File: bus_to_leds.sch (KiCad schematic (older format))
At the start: 32 parts

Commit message: ram pcb
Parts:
- R0: renamed from R1; value 220 -> 5k
- R1: renamed from R2; value 220 -> 5k
- R10: renamed from R11; value 220 -> 5k
- R11: renamed from R12; value 220 -> 5k
- R12: renamed from R13; value 220 -> 5k
- R13: renamed from R14; value 220 -> 5k
- R14: renamed from R15; value 220 -> 5k
- R15: renamed from R16; value 220 -> 5k
- R2: renamed from R3; value 220 -> 5k
- R3: renamed from R4; value 220 -> 5k
- R4: renamed from R5; value 220 -> 5k
- R5: renamed from R6; value 220 -> 5k
- R6: renamed from R7; value 220 -> 5k
- R7: renamed from R8; value 220 -> 5k
- R8: renamed from R9; value 220 -> 5k
- R9: renamed from R10; value 220 -> 5k
- renumbered D1 to D0, D2 to D1, D11 to D10, D12 to D11, D13 to D12, D14 to D13, D15 to D14, D16 to D15, D3 to D2, D4 to D3, D5 to D4, D6 to D5, D7 to D6, D8 to D7, D9 to D8, D10 to D9

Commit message: way to long since last commit
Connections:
- net D0: now also D15.2 (A); no longer D0.2 (A)
- net D1: now also D14.2 (A); no longer D1.2 (A)
- net D10: now also D5.2 (A); no longer D10.2 (A)
- net D11: now also D4.2 (A); no longer D11.2 (A)
- net D12: now also D3.2 (A); no longer D12.2 (A)
- net D13: now also D2.2 (A); no longer D13.2 (A)
- net D14: now also D1.2 (A); no longer D14.2 (A)
- net D15: now also D0.2 (A); no longer D15.2 (A)
- net D2: now also D13.2 (A); no longer D2.2 (A)
- net D3: now also D12.2 (A); no longer D3.2 (A)
- net D4: now also D11.2 (A); no longer D4.2 (A)
- net D5: now also D10.2 (A); no longer D5.2 (A)
- net D6: now also D9.2 (A); no longer D6.2 (A)
- net D7: now also D8.2 (A); no longer D7.2 (A)
- net D8: now also D7.2 (A); no longer D8.2 (A)
- net D9: now also D6.2 (A); no longer D9.2 (A)
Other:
- moved on the sheet: D0, D1, D10, D11, D12, D13, D14, D15, D2, D3, D4, D5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

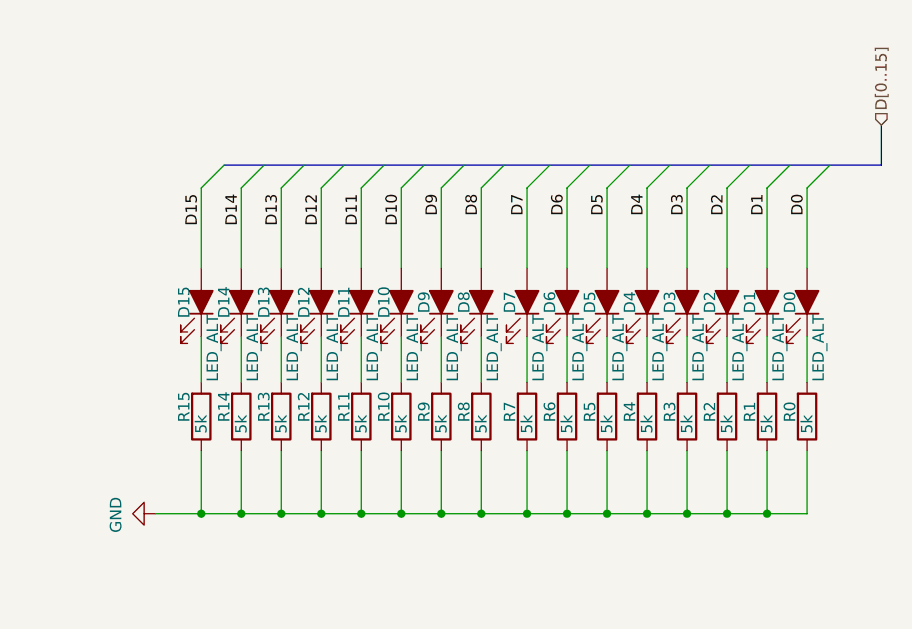
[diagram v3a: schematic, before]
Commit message: add bit operations
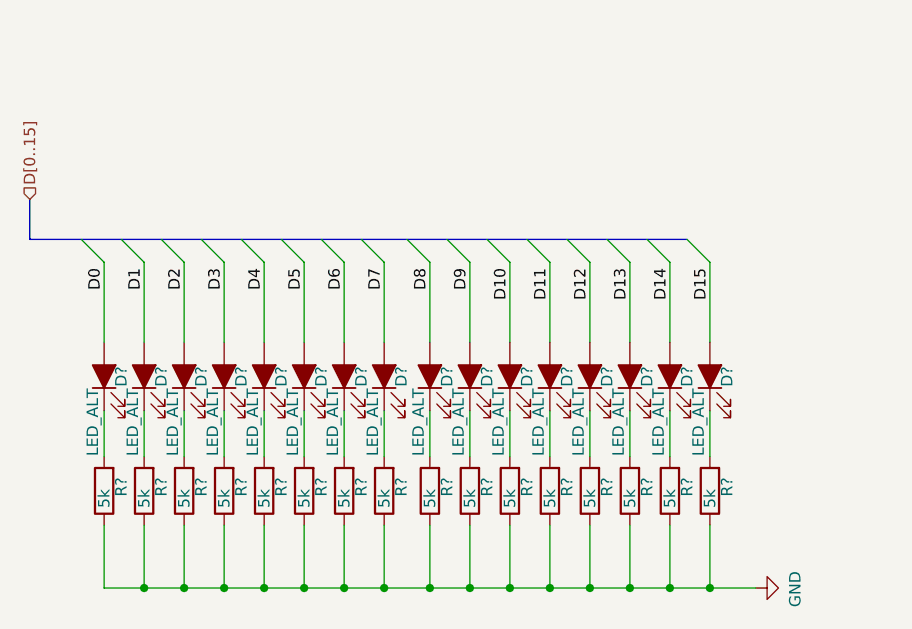
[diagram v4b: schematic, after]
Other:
- moved on the sheet: D?, R?

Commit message: memory programmer and cu
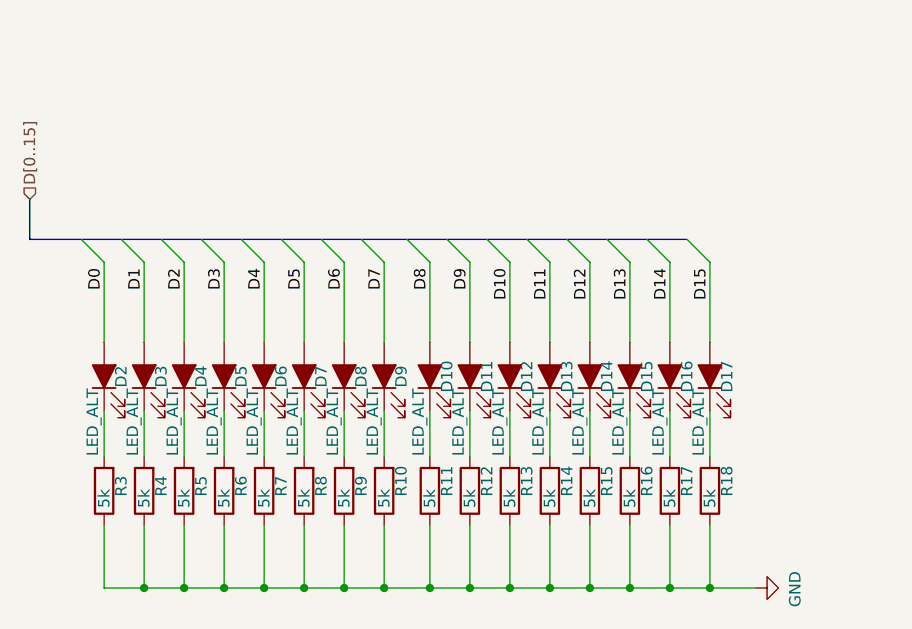
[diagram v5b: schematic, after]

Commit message: connect cu and start creating material csv
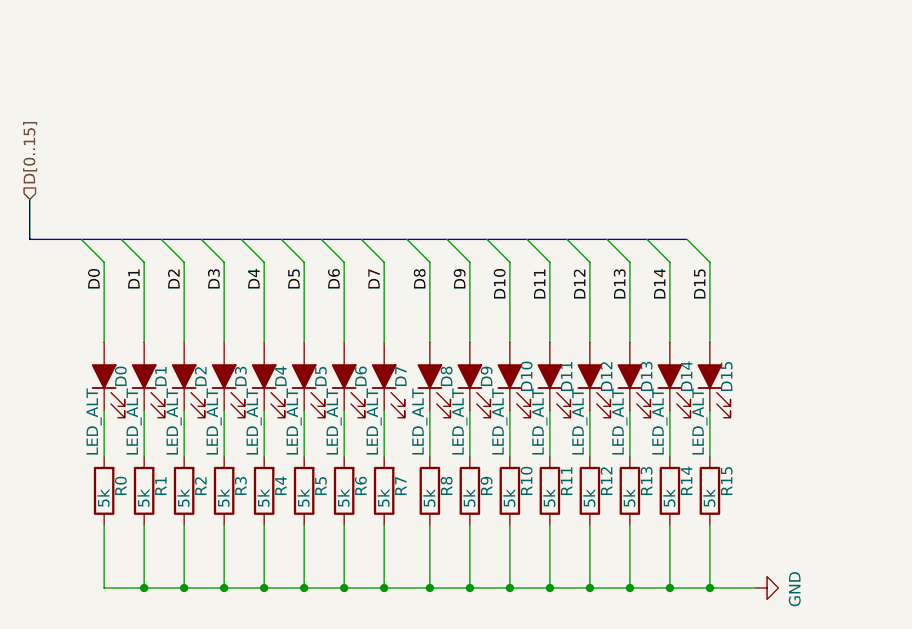
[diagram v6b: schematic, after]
